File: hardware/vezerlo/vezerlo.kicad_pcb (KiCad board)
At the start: 4 copper layers, 68 x 86.5 mm, 158 parts, among them J1 24V IN, J2 BUS (XH), J3 BUS (XH), J4 USB-C 16P, J5 DEBUG, J6 HR911105A, J7 u.FL, J8 BŐVÍTŐ, SW1 RESET, SW2 BOOT, U1 LMR36015BRNXR, U10 E22-900M22S, U11 74LVC1G04, U12 LM66200DRLR, U2 LMR33630ADDA, U3 TPS259531DSGR, U4 ESP32-C6-WROOM-1-N16, U5 W5500, U6 TCAN1044AVDRQ1, U7 ESD2CAN24-Q1, U8 USBLC6-2SC6, U9 74HCT14D, Y1 25MHz ±30ppm

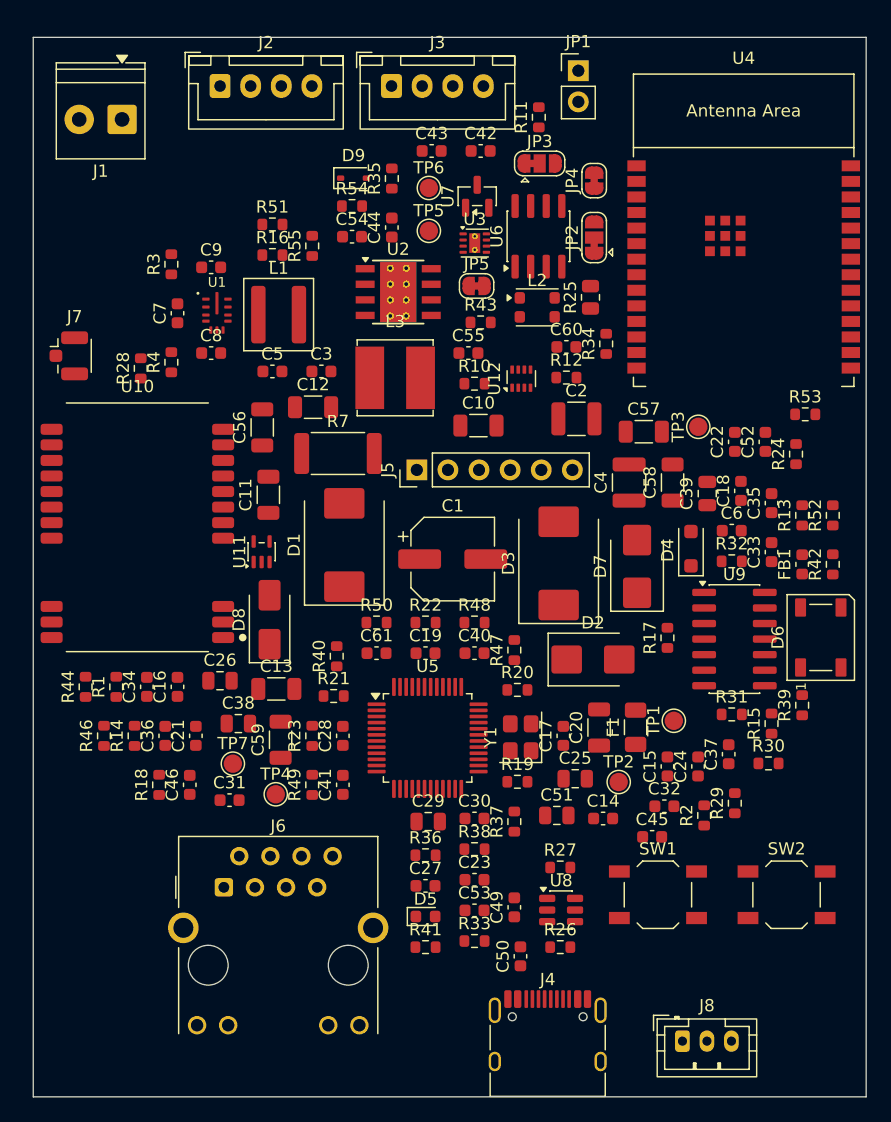
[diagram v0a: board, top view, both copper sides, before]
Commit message: Hardver: szakértői javítások (D74–D77), STM32L433 + SN65HVD230 + GND-ági polaritásvédelem (D78–D81), teljes ellenőrzés
- D74–D77: busz-GND ellenállás, CAN-fojtó-hely, TVS a +5V_BUCK-on és a VUSB-n, bemenetvédelem,
  230 V-os és antenna-tiltás a NYÁK-on, SCT-jack footprint
- D78–D80: modul-MCU STM32L433RCT3 (VIN_SENSE PB1, LED: TIM15/TIM16, I_SENSE PA3), modul-transceiver
  SN65HVD230, N-FET a GND-ágban (vezérlő Q1, LED Q201, relé Q100), MCP9701A, táp-LED a +5V-ról,
  2 oz a LED-/relémodulon, AP2112K marad; D81 javaslat (TPD4E02B04 a bemeneteken)
- CubeMX-projektek L433-ra, fejsoros kódgenerálással ellenőrizve (minden periféria inicializálódik)
- gen/ellenorzes.py (ERC, láb ↔ pad, modulmag, CubeMX, polaritásvédelem, NYÁK ↔ rajz, DRC) – 0 hiba
- gen/bom.sh + bom/*.csv darabjegyzék; docs/komponenslista.md a konzulensnek
- kontextus: DONTESEK D74–D81, specifikációk, ATTEKINTES, NAPLO, beszerzési lista; alkatrészkészlet-jegyzet (claude.ai)

Co-Authored-By: Claude Opus 5.5 <noreply@anthropic.com>
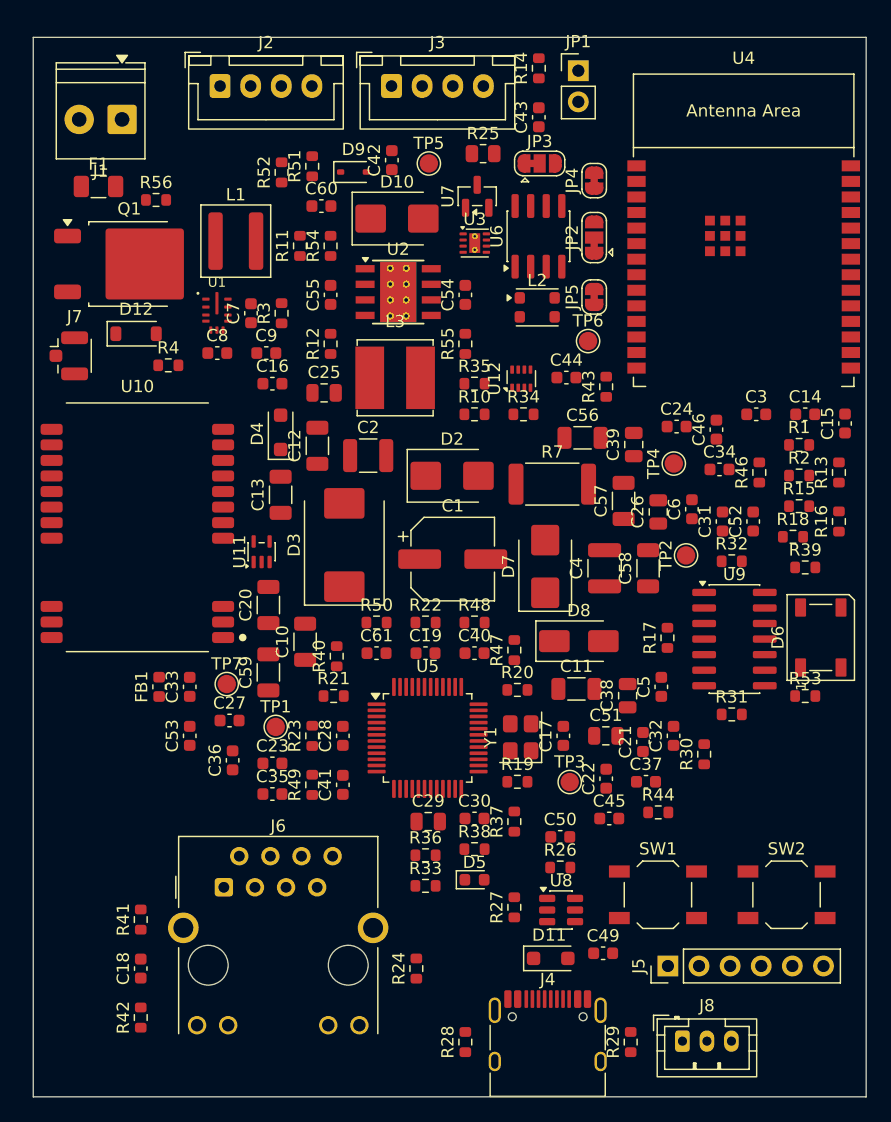
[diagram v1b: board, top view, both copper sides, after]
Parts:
- removed D1: B360, Diode_SMD:D_SMC
- added D10: SMBJ6.0A, Diode_SMD:D_SMB, F.Cu at (129.7, 114.8)
- added D11: SMF5.0A, Diode_SMD:D_SOD-123F, F.Cu at (142.2, 175.2)
- added D12: BZT52C15, Diode_SMD:D_SOD-123, F.Cu at (108.4, 124.2)
- added Q1: IRFR1205, Package_TO_SOT_SMD:TO-252-2, F.Cu at (107.8, 118.5)
- added R56: 10k, Resistor_SMD:R_0603_1608Metric, F.Cu at (110.0, 113.3)
- moved R42 67.5 mm to (108.8, 180.0)
- moved R14 63.7 mm to (141.3, 102.5)
- moved C18 62.6 mm to (108.8, 176.0)
- moved F1 62.2 mm to (105.3, 112.2), turned to 0 degrees
- moved R28 61.1 mm to (135.3, 182.0)
- moved R1 59.1 mm to (162.5, 133.3), turned to 0 degrees
- moved R46 57.7 mm to (159.3, 135.5)
- moved R18 55.6 mm to (162.0, 140.8), turned to 0 degrees
- moved FB1 53.4 mm to (110.3, 153.0)
- moved R52 53.0 mm to (120.3, 111.0)
- moved R24 52.2 mm to (131.3, 176.0)
- moved C46 51.9 mm to (155.8, 132.0)
- moved R16 51.1 mm to (165.8, 139.5), turned to 90 degrees
- moved C34 50.0 mm to (156.0, 135.3), turned to 0 degrees
- moved C33 48.8 mm to (112.8, 153.0)
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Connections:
- F1 pad 2: Net-(D1-A) -> /+24V_P
- J1 pad 2: GND -> /GND_IN
- R44 pad 1: +3V3 -> +5V

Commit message: Hardver: determinisztikus UUID-k – a NYÁK-footprintek újra a rajzi szimbólumokra mutatnak
- kigen: a szimbólum-UUID a projekt + hivatkozási jel alapján (uuid5), a többi elemé laponként sorszámból –
  két generálás bájtra azonos fájlt ad, és az újragenerálás nem töri el a „Update PCB from Schematic”-ot (D67)
- a négy NYÁK újragenerálva: mind a 581 footprint a saját szimbólumára mutat (előtte egy sem)
- ellenorzes.py: új ellenőrzés a NYÁK ↔ rajz szimbólum-kapcsolatra; teljes futás: 0 hiba
- README, NAPLO

Co-Authored-By: Claude Opus 5.5 <noreply@anthropic.com>
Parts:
- moved R51 51.9 mm to (165.8, 139.5)
- moved R52 51.3 mm to (162.0, 140.8), turned to 0 degrees
- moved R18 43.5 mm to (141.3, 102.5), turned to 90 degrees
- moved R14 41.1 mm to (165.8, 135.5)
- moved C15 35.6 mm to (155.0, 165.3), turned to 0 degrees
- moved R16 26.1 mm to (161.5, 165.3), turned to 0 degrees
- moved R15 25.6 mm to (155.0, 162.8)
- moved R53 10.5 mm to (163.0, 143.3)
- moved R39 5.02 mm to (162.5, 138.3)
- moved R1 4.14 mm to (166.3, 131.5), turned to 90 degrees
- moved R13 3.26 mm to (162.5, 135.8), turned to 0 degrees
- moved R2 2.50 mm to (162.5, 133.3)

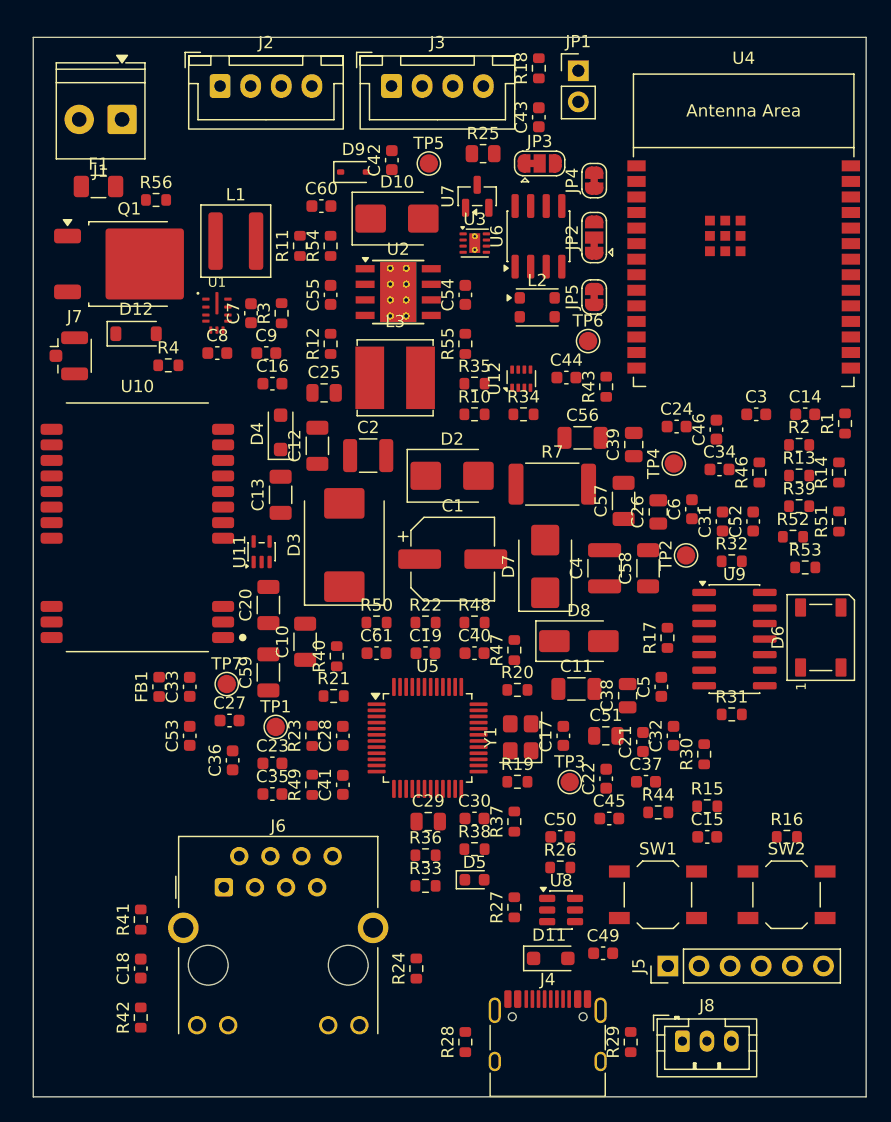
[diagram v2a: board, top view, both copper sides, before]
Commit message: Hardver: legolcsóbb beszerzés (D84) – Hestore + DigiKey, a rajz a kapható típusokra igazítva; beszerzési lista
- gen/beszerzes.py → bom/beszerzes.csv: BOM-tételenként forrás, Hestore-kód, nettó ár, készlet
- J1/J100 Degson DG250, J201 DG128 (15 A), J202–J204 KF128, F201 15 A; L1/L3 HPI0630 (saját footprint);
  R209 CRE2512; C40/C41 12 pF; ESP32-C6-WROOM-1-N8; SS56C, BAT54HT1G, STPS3L60U, BLM18EG221
- NYÁK-ok újragenerálva (a layout még nem indult el); bekötés változatlan, ellenorzes.py: 0 hiba
- SAMPLE-KERESEK: az NTMFS5C604NL nincs kézben (javítva)

Co-Authored-By: Claude Opus 5.5 <noreply@anthropic.com>
Claude-Session: https://claude.ai/code/session_01KVtZMUPbtveTXy9VyJshyt
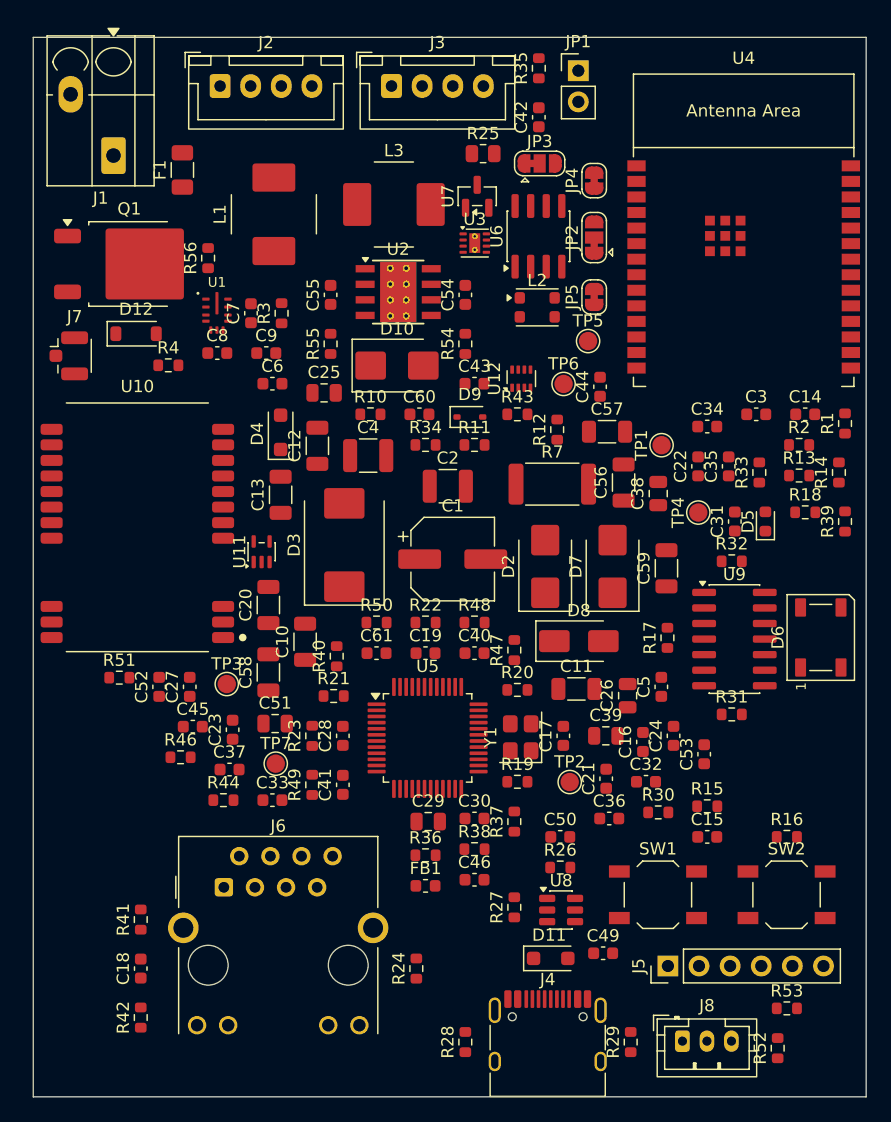
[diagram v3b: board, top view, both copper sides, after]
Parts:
- C4: value 4µ7/50V -> 10µ/50V
- C40, C41: value 18p -> 12p
- C9: value 20p -> 22p
- D3: value B360 -> SS56C
- D9: value BAT54WS -> BAT54HT1G
- FB1: value 120R@100MHz -> BLM18EG221
- J1: footprint TerminalBlock_Phoenix:TerminalBlock_Phoenix_PT-1,5-2-3.5-H_1x02_P3.50mm_Horizontal -> TerminalBlock_Degson:TerminalBlock_Degson_DG250-3.5-02P_1x02_P3.50mm_45Degree
- L1: footprint Inductor_SMD:L_Coilcraft_XAL5030-XXX -> modularis:L_FerroCore_HPI0630
- L3: footprint Inductor_SMD:L_Bourns_SRN6045TA -> modularis:L_FerroCore_HPI0630
- U4: value ESP32-C6-WROOM-1-N16 -> ESP32-C6-WROOM-1-N8
- moved R51 60.1 mm to (107.0, 152.3), turned to 0 degrees
- moved R46 52.7 mm to (112.0, 158.8), turned to 0 degrees
- moved C52 50.3 mm to (110.3, 153.0)
- moved C35 45.9 mm to (156.8, 135.0), turned to 90 degrees
- moved R33 43.4 mm to (159.3, 135.5), turned to 90 degrees
- moved R18 42.3 mm to (163.0, 138.8), turned to 0 degrees
- moved C16 42.1 mm to (149.8, 157.5), turned to 90 degrees
- moved C53 42.0 mm to (154.8, 158.5)
- moved R52 41.8 mm to (160.8, 182.5), turned to 90 degrees
- moved C46 41.7 mm to (136.0, 168.8), turned to 0 degrees
- moved TP1 39.0 mm to (151.3, 133.3), turned to 90 degrees
- moved D5 37.7 mm to (159.8, 139.5), turned to 90 degrees
- moved R53 36.0 mm to (161.5, 179.3)
- moved C6 35.8 mm to (119.5, 128.3), turned to 0 degrees
- moved R44 35.5 mm to (115.5, 162.3)
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
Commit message: Hardver: legolcsóbb beszerzés LCSC-ről (D85), megszűnt FET-ek pótlása, LCSC-kosárlista
- gen/lcsc.py: LCSC-árak a JLC alkatrészkeresőjéből; gen/beszerzes.py soronként a legolcsóbb forrás (Hestore / LCSC, ÁFA-val)
- bom/lcsc-kosar.csv: 99 tétel (~15 eFt), az LCSC BOM Tooljába feltölthető; házak később, ST-Link/Nucleo kézben
- Q202–Q207 NTD5C648NL → NCE6080K, Q201 NTMFS5C604NL → NCEP6090AGU (nem kaphatók), F201 → NANO² 15 A,
  D211–D216 SS56B, J1/J100 DG128, L1/L3 LCSC-s 0630-as tekercs, kis ESR-ű kvarcok
- bekötés változatlan (netlista 0 / 0), ellenorzes.py: 0 hiba

Co-Authored-By: Claude Opus 5.5 <noreply@anthropic.com>
Claude-Session: https://claude.ai/code/session_01KVtZMUPbtveTXy9VyJshyt
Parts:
- J1: footprint TerminalBlock_Degson:TerminalBlock_Degson_DG250-3.5-02P_1x02_P3.50mm_45Degree -> TerminalBlock_Phoenix:TerminalBlock_Phoenix_MKDS-1,5-2_1x02_P5.00mm_Horizontal
- moved R33 51.3 mm to (115.5, 162.3), turned to 0 degrees
- moved C27 46.8 mm to (154.5, 131.8), turned to 0 degrees
- moved C34 46.8 mm to (119.5, 162.3)
- moved C33 45.8 mm to (156.3, 135.0), turned to 90 degrees
- moved R46 44.3 mm to (156.3, 158.5), turned to 90 degrees
- moved C22 43.7 mm to (116.3, 156.5)
- moved TP3 41.0 mm to (154.3, 138.8), turned to 90 degrees
- moved FB1 40.7 mm to (159.8, 139.5), turned to 90 degrees
- moved C45 40.4 mm to (153.3, 160.0), turned to 90 degrees
- moved C6 40.3 mm to (151.3, 153.0), turned to 90 degrees
- moved TP4 40.1 mm to (119.8, 159.3), turned to 0 degrees
- moved C5 38.8 mm to (118.3, 132.5)
- moved C51 38.7 mm to (151.0, 133.2), turned to 90 degrees
- moved C25 35.0 mm to (148.5, 153.7), turned to 90 degrees
- moved D4 33.4 mm to (151.7, 143.2)
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
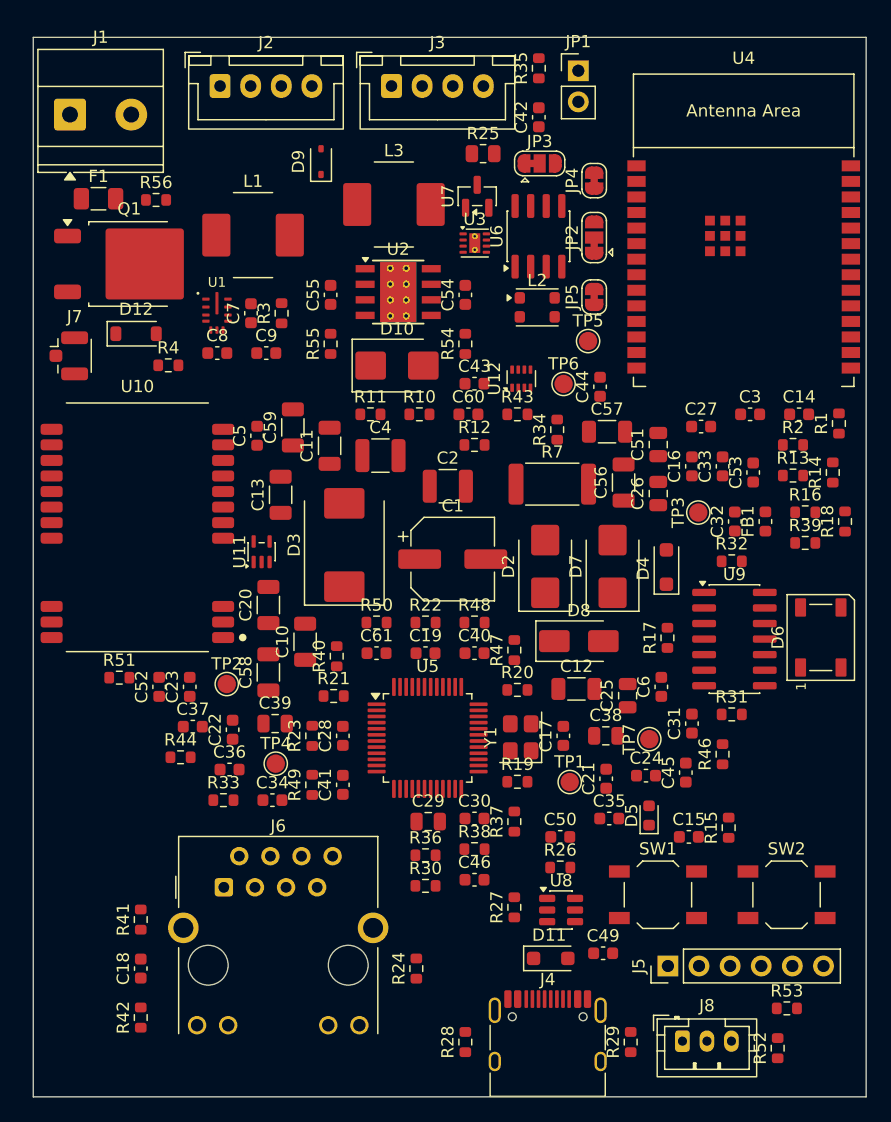
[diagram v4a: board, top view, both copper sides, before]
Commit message: Hardver: layout-előkészítés (D86) – JLC-szabályok és via-méretek, modulmag-blokk, a modulok elrendezése
- laponként .kicad_dru: JLC 4 réteg / 1 oz; via 0,3/0,45 (jel), 0,4/0,7 (táp), 0,6/1,0 mm (15 A); 230 V ↔ SELV 8 mm
- modulmag-blokk mindhárom modulon azonos relatív elrendezéssel (átvihető layout), 0,25 mm-es rács
- a sorkapcsok a Gainta D4MG fedélfurataira igazítva (5,08 mm), a kötött helyű alkatrészek zárolva
- LED-modul: LED-sor, meghajtók, FET-sor; relé: betáp és LED-sor; bemeneti: csatornánkénti oszlopok, ESD-sor
- lábhoz rendelés: hidegítők a tápjukhoz, gate-ellenállások a gate-hez; a vezérlő elrendezése még hátra (U4)
- docs/d4mg.pdf: a ház rajza; ellenorzes.py: 0 hiba

Co-Authored-By: Claude Opus 5.5 <noreply@anthropic.com>
Claude-Session: https://claude.ai/code/session_01KVtZMUPbtveTXy9VyJshyt
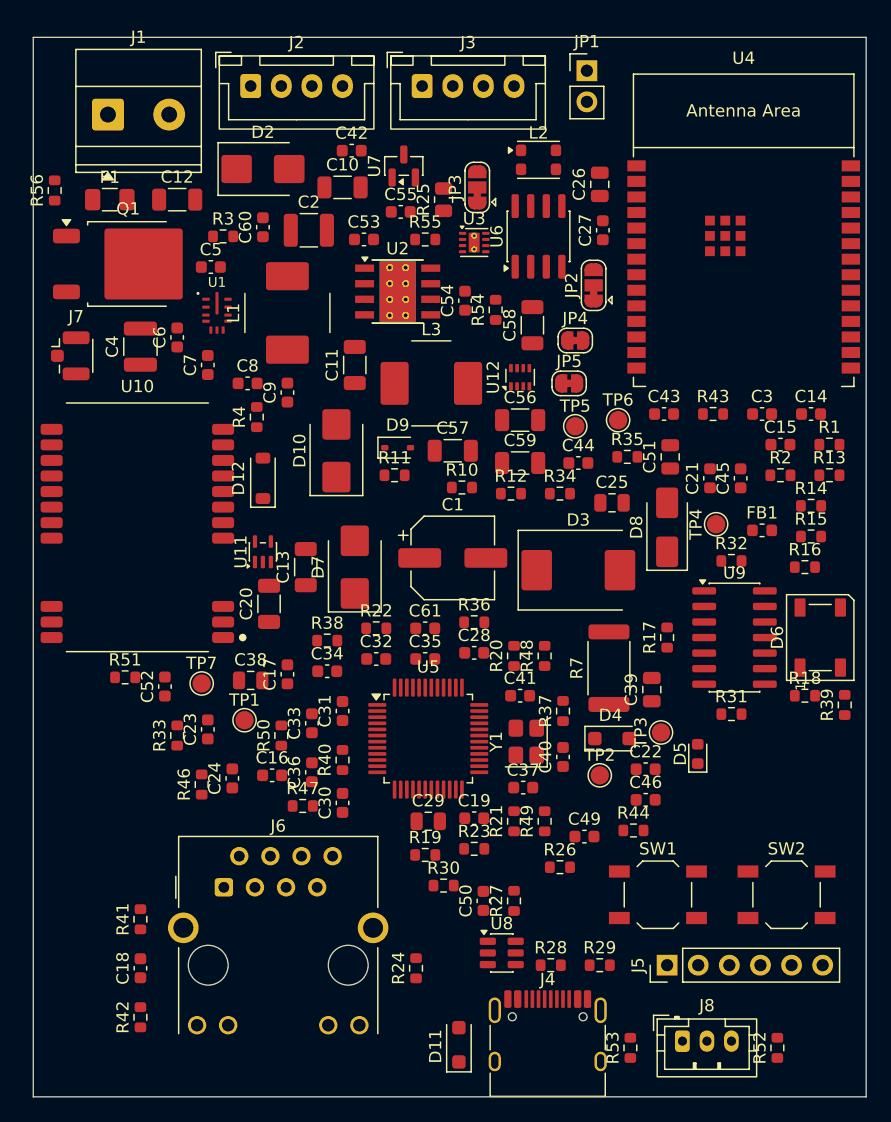
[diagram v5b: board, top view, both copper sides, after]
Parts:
- moved C12 51.6 mm to (111.8, 113.2)
- moved C6 48.7 mm to (111.8, 124.5)
- moved R46 42.6 mm to (113.8, 161.0)
- moved C16 42.6 mm to (119.5, 160.2), turned to 0 degrees
- moved TP4 40.9 mm to (155.8, 139.8), turned to 90 degrees
- moved D2 39.8 mm to (118.8, 110.8), turned to 0 degrees
- moved C33 39.5 mm to (122.8, 156.0)
- moved R44 37.5 mm to (149.0, 164.8)
- moved C10 37.2 mm to (125.2, 112.2), turned to 0 degrees
- moved C53 37.0 mm to (127.0, 116.5), turned to 0 degrees
- moved TP7 36.8 mm to (113.8, 152.8), turned to 0 degrees
- moved C58 35.6 mm to (140.8, 123.5)
- moved C22 33.9 mm to (150.0, 159.8), turned to 0 degrees
- moved C24 33.8 mm to (116.2, 160.5), turned to 90 degrees
- moved C15 32.9 mm to (161.0, 133.2)
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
